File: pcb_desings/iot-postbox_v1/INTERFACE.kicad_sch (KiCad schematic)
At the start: 25 parts, among them J2 JTAG, J3 LED, J6 EXT1, J7 EXT2, SW1 SW1, SW2 SW2, SW3 BOOT, SW4 RST, U4 RFM95W-868S2

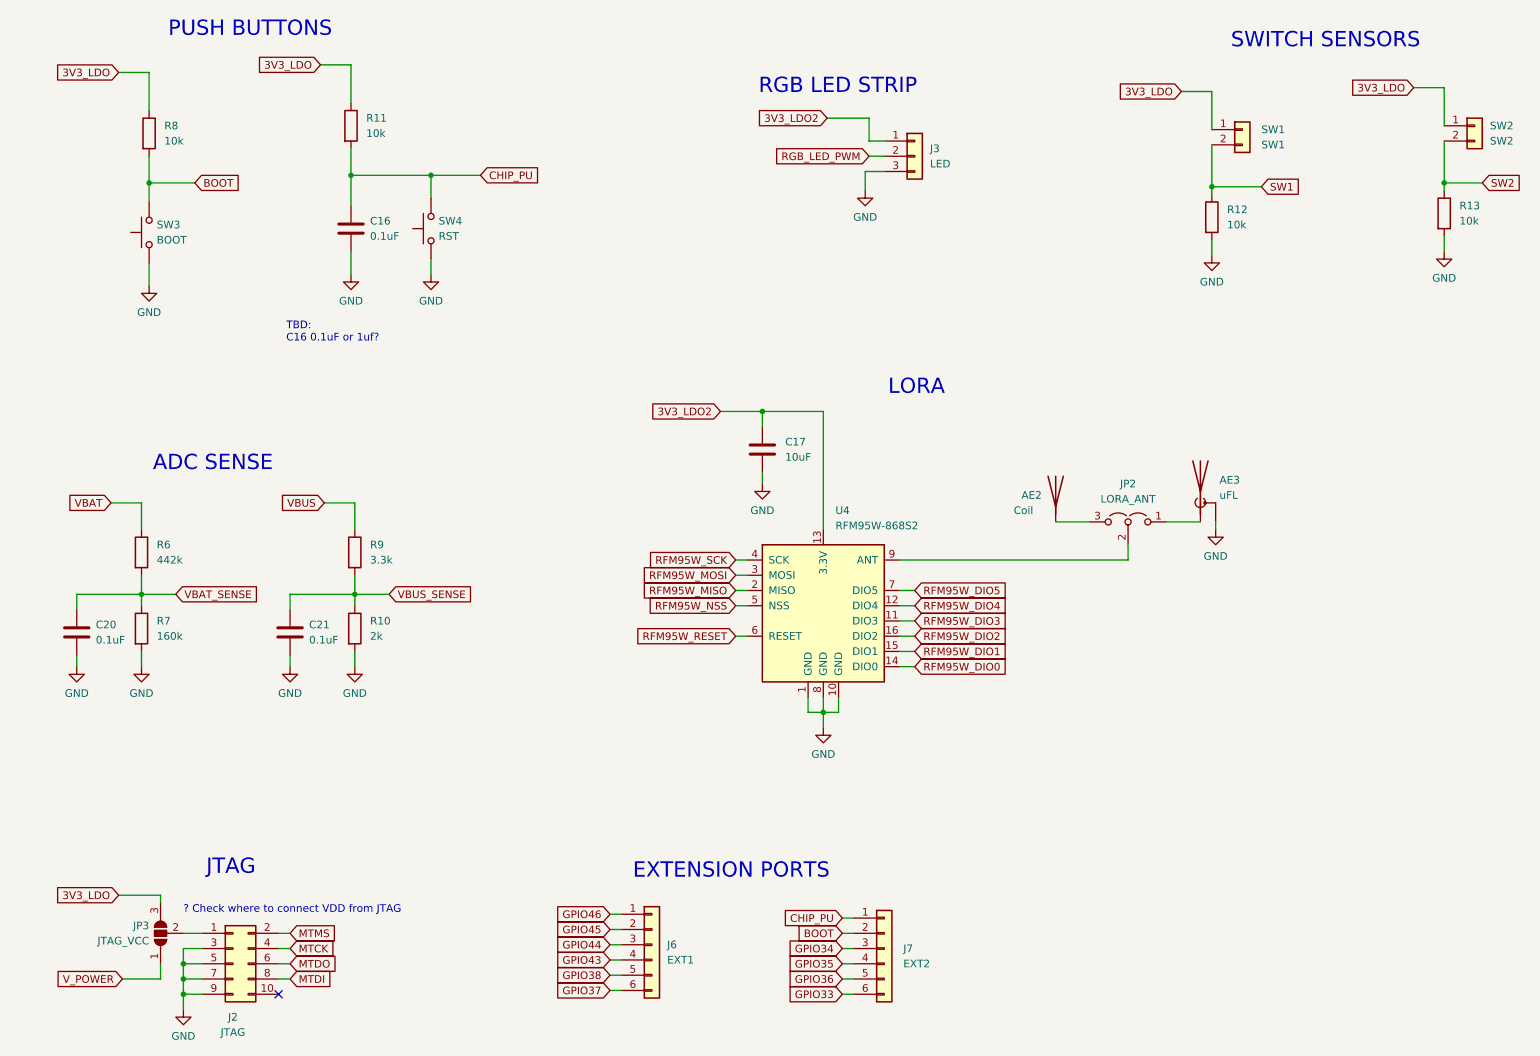
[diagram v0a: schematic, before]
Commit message: Added iot-postbox_v1 sch to v1.1. Added minor documentation
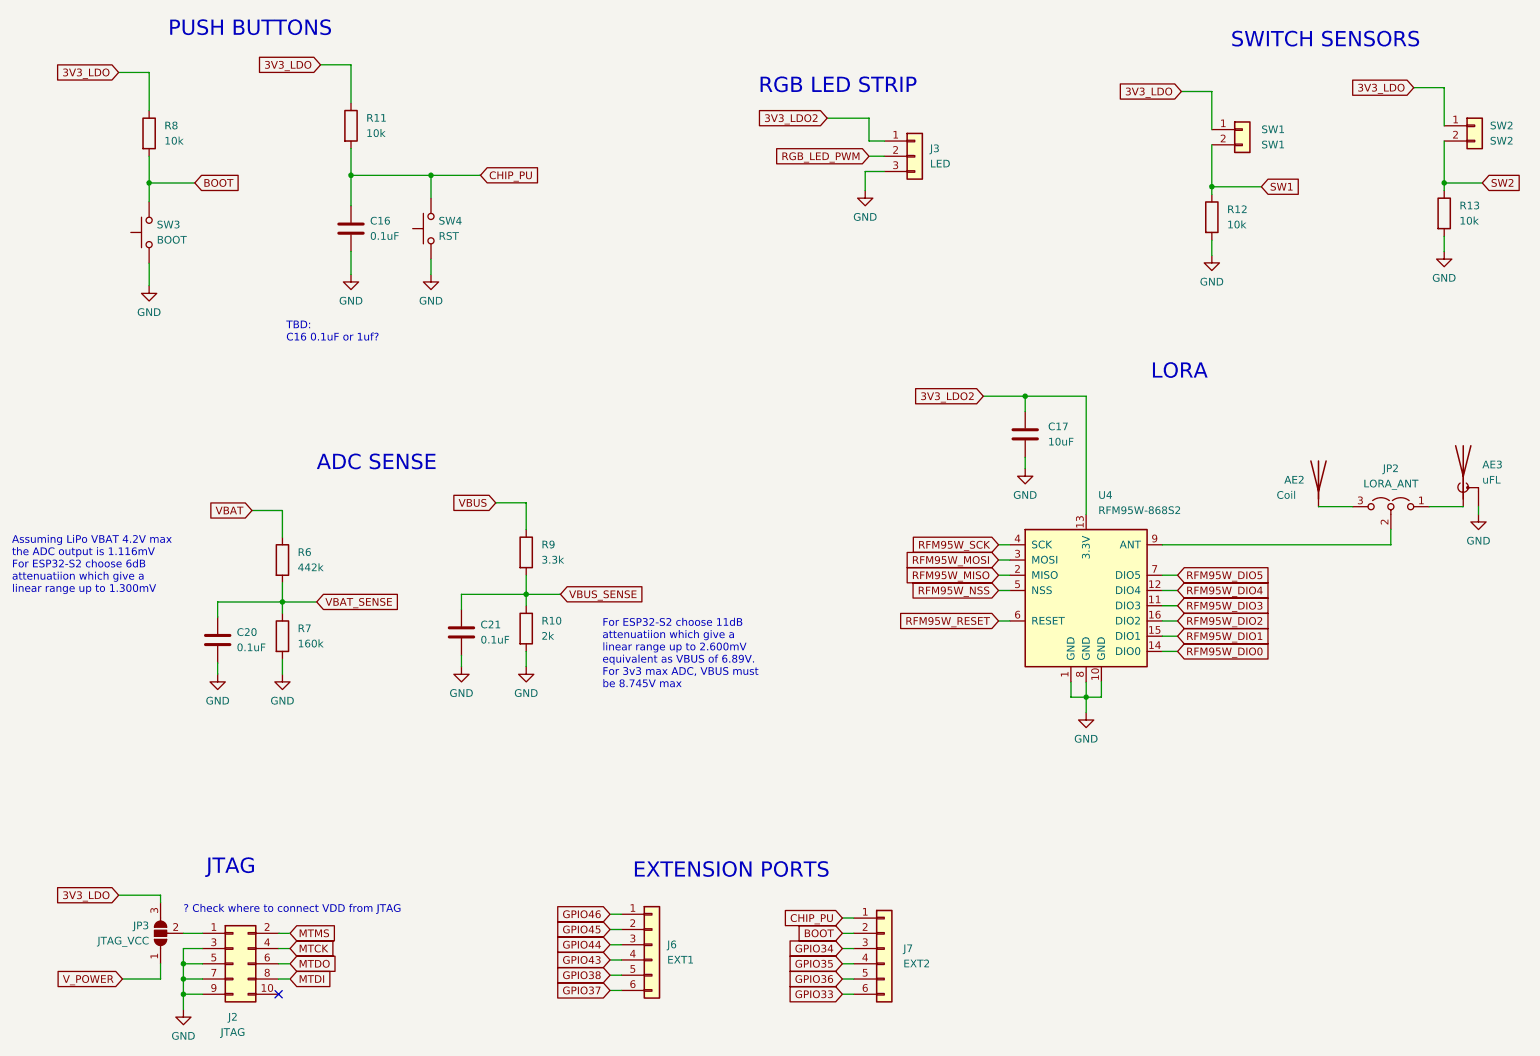
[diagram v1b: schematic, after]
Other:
- note added: "Assuming LiPo VBAT 4.2V max the ADC output is 1.116mV For ESP32-S2 choose 6dB attenuatiion which give a linear range up to 1.300mV"
- note added: "For ESP32-S2 choose 11dB attenuatiion which give a linear range up to 2.600mV equivalent as VBUS of 6.89V. For 3v3 max ADC, VBUS must be 8.745V max"
- moved on the sheet: AE2, AE3, C17, C20, C21, JP2, R10, R6, R7, R9, U4

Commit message: Created iot-postbox v1.2 migrating to kicad v9. Fixed missing 3d designs, replaced horizontal footprints for some connectors.
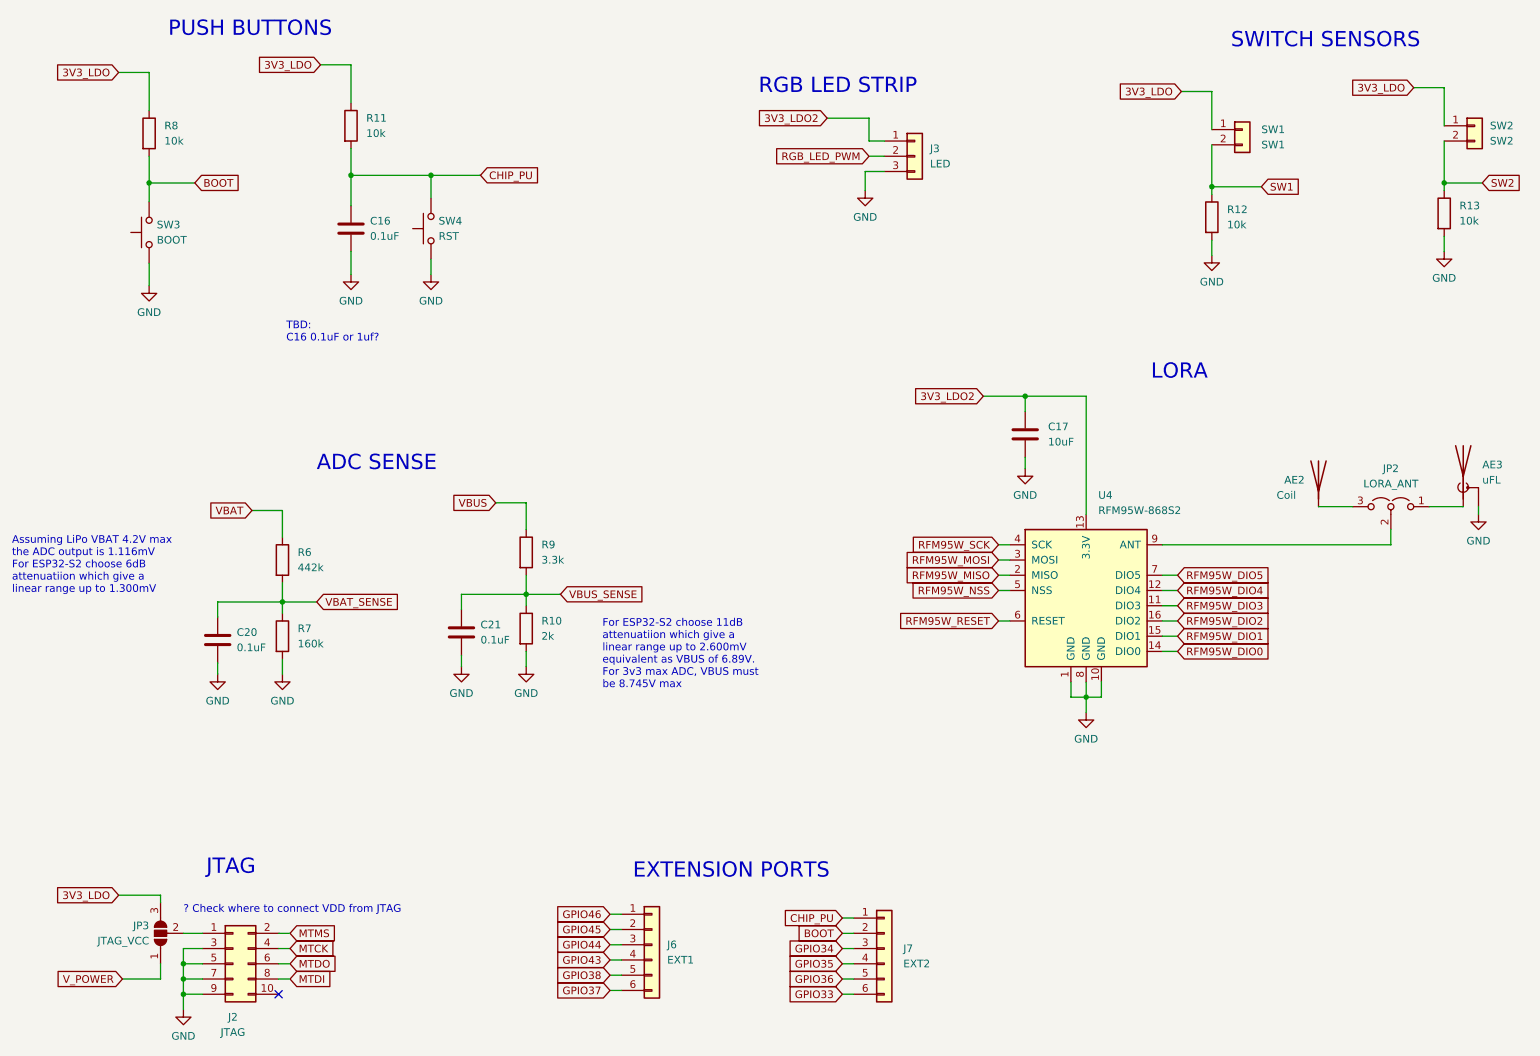
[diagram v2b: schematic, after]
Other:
- company: (none) -> @paclema
